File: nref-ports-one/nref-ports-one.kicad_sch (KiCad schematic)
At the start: 155 parts, among them J1 CONN_HEAD, J10 CONN_SPK, J11 POWSW, J12 SBU, J2 DM3AT-SF-PEJM5, J3 09452812561, J4 USB_C_Receptacle, J5 Conn_01x10_Pin, J6 Conn_01x14_Pin, J7 Conn_01x12_Pin, J8 PWR, J9 Conn_01x10_Pin, SW1 SW_Push, U1 TPS7A0533PDBZ, U10 LMR51430, U11 TPS66021YBGR, U12 TLV75518PDBV, U13 TMUXHS4212, U14 EQCO5X31C0-I_6NX, U15 LP5907MFX-1.2, U2 TLV320AIC3100, U3 TXS0108EPW, U4 SN74AVC1T45, U5 TPD4E02B04DQA, U6 TPD4E02B04DQA, U7 TPD4E02B04DQA, U8 FUSB302BMPX, U9 PCA9557RGVR

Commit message: commit various notes / polishing for ports-one and ports-two
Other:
- note added: ""In single-lane mode, only the differential pairs closest to the CC pin are used for data transmission""
- note added: "- if CC2 is pulled down: cable flipped - if CC1 is pulled down: cable unflipped"
- note added: "- if SEL high"
- note added: "- if SEL low"
- note added: "- if SEL low: Port A to Port B - if SEL high: Port A to Port C"
- note added: "A10"
- note added: "A11"
- note added: "A2"
- note added: "A3"
- note added: "B10"
- note added: "B11"
- note added: "B2"
- note added: "B3"
- note added: "pol. swapped on purpose!"
- note removed: "pair swapped on purpose!"

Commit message: ports-one: add TODOs after hw debugging
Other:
- note added: "TODO: P0 is open drain! swap SRC and SINK EN!"
- note added: "TODO: not 3v3 on 66021! (3v3 on 66020)"
- note added: "TODO: remove!!"
- note added: "TODO: remove, internal pulldown"
- note added: "TODO: wrong pinout/footprint"
- note added: "required to start the mechanism"
- note removed: "TODO: possibly 0R"

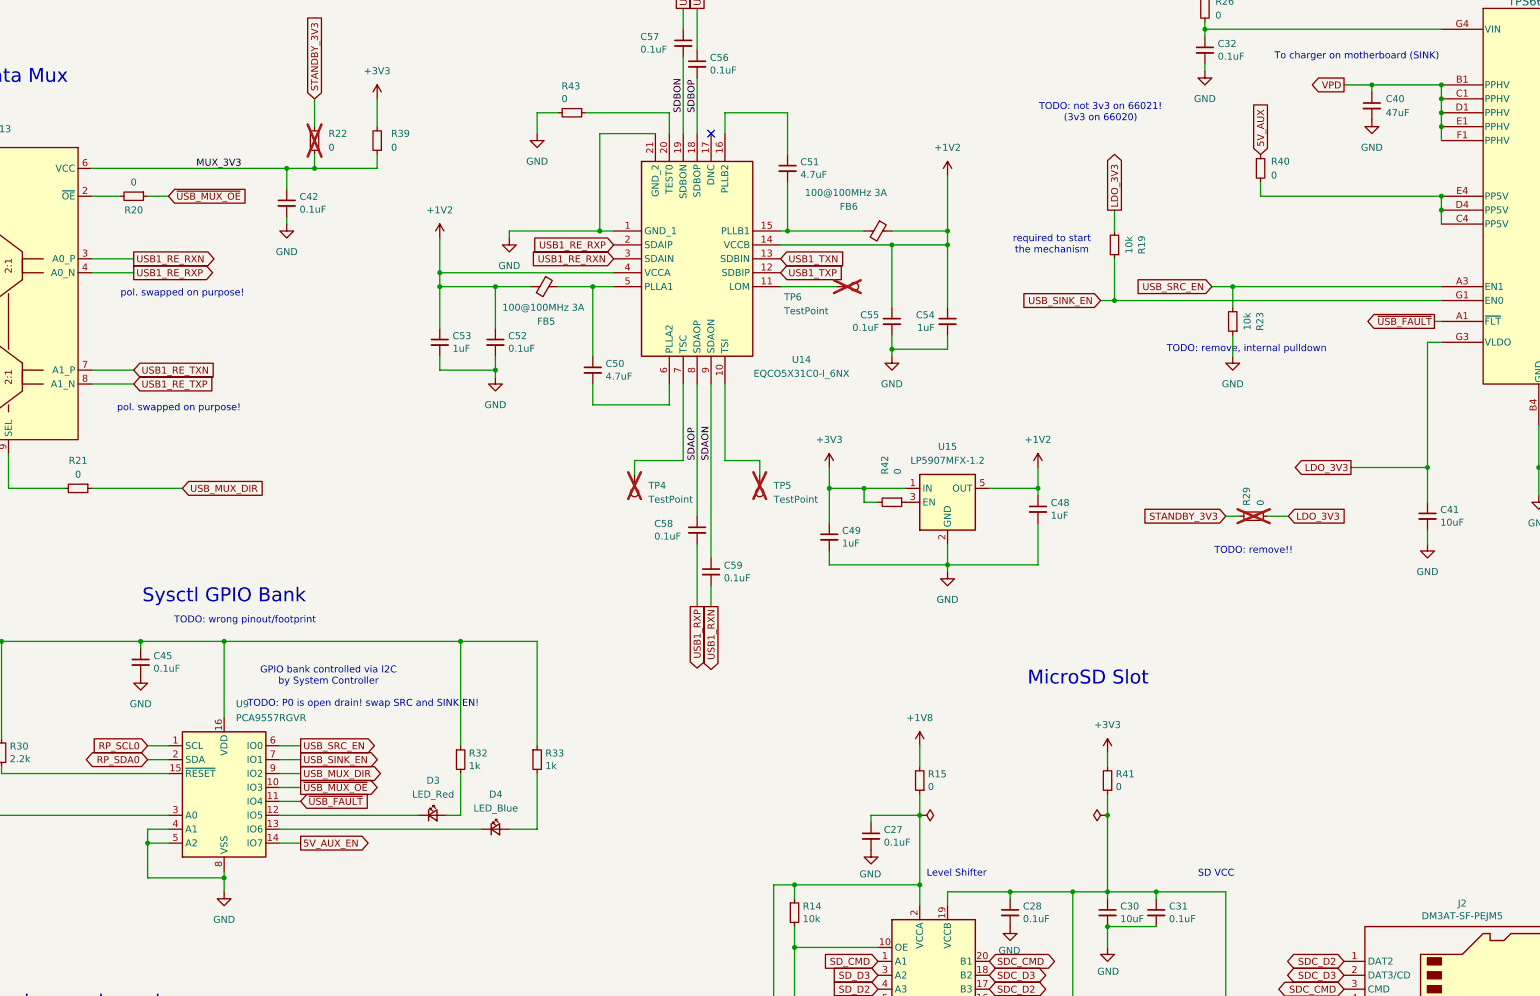
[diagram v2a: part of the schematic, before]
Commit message: ports-one: fix u9 pinout; remove r23
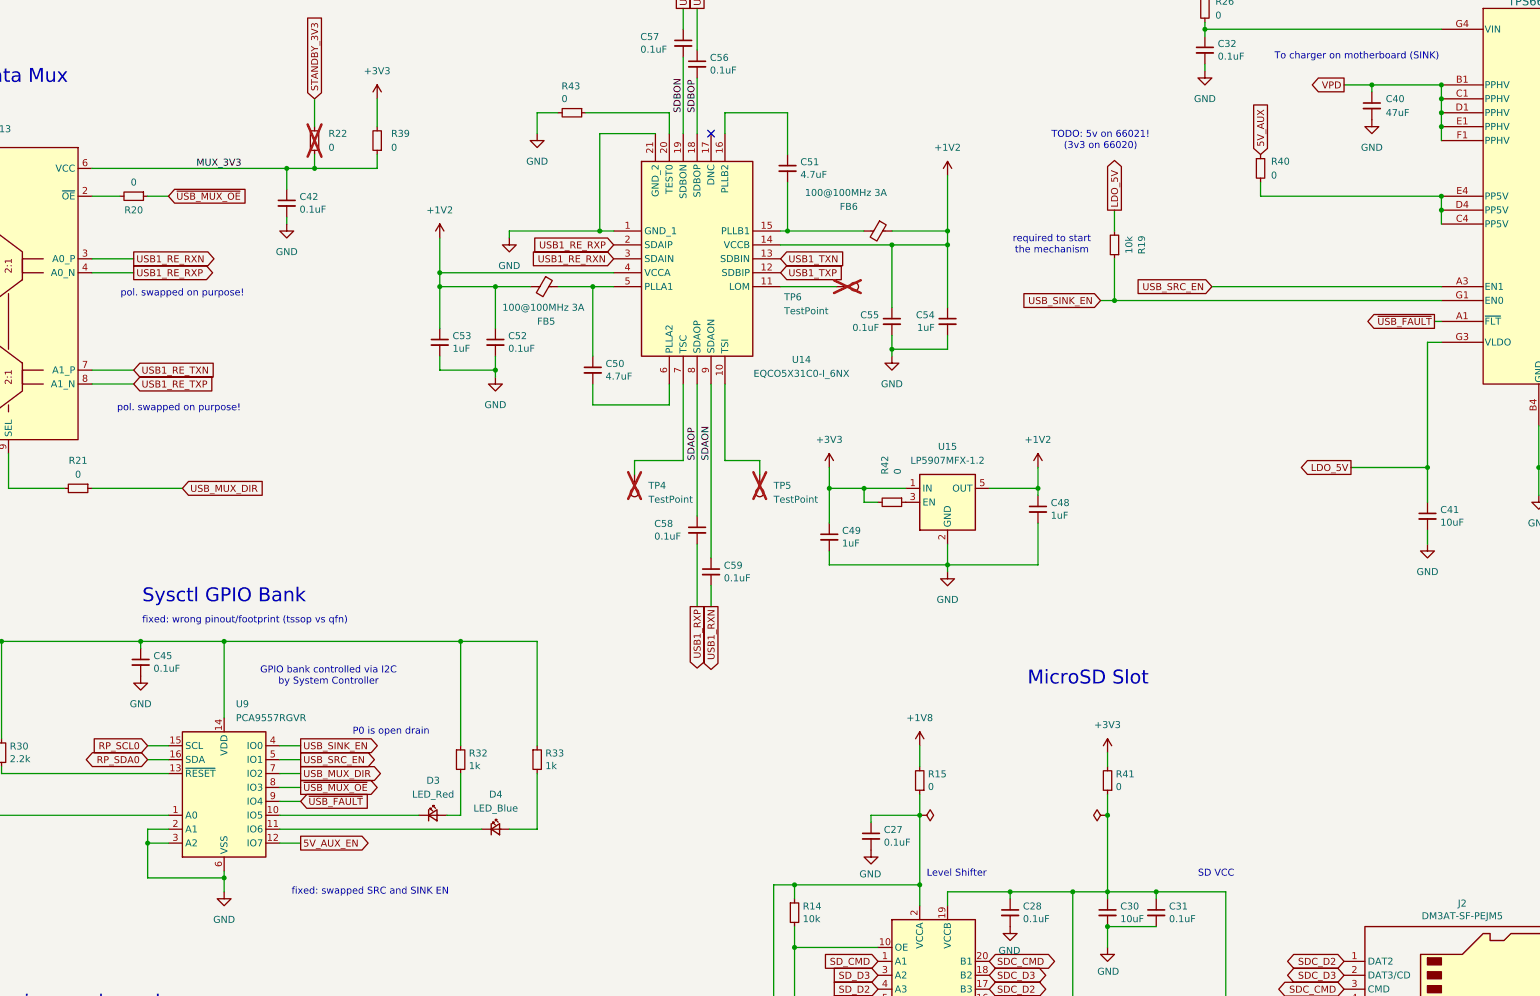
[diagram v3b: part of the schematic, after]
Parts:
- removed R23: 10k, Resistor_SMD:R_0402_1005Metric, symbol Device:R_Small
- removed R29: 0, Resistor_SMD:R_0402_1005Metric, symbol Device:R_Small
- U9: symbol Interface_Expansion:PCA9557PW -> Interface_Expansion:PCA9557BS
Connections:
- net 5V_AUX_EN: now also U9.12 (IO7); no longer U9.14 (IO7)
- net GND: now also U9.2 (A1), U9.3 (A2), U9.6 (VSS); no longer U9.4 (A1), U9.5 (A2), U9.8 (VSS)
- net RP_SCL0: now also U9.15 (SCL); no longer U9.1 (SCL)
- net RP_SDA0: now also U9.16 (SDA); no longer U9.2 (SDA)
- net STANDBY_3V3: now also U9.14 (VDD); no longer U9.16 (VDD)
- net USB_MUX_DIR: now also U9.7 (IO2); no longer U9.9 (IO2)
- net USB_SINK_EN: now also U9.4 (IO0); no longer U9.7 (IO1)
- net USB_SRC_EN: now also U9.5 (IO1); no longer U9.6 (IO0)
- net ~{USB_FAULT}: now also U9.9 (IO4); no longer U9.11 (IO4)
- net ~{USB_MUX_OE}: now also U9.8 (IO3); no longer U9.10 (IO3)
- net at D3.1 (K): now also U9.10 (IO5); no longer U9.12 (IO5)
- net at R30.2: now also U9.13 (~{RESET}); no longer U9.15 (~{RESET})
- net at D4.1 (K): now also U9.11 (IO6); no longer U9.13 (IO6)
- net at R31.2: now also U9.1 (A0); no longer U9.3 (A0)
- net LDO_3V3 renamed LDO_5V
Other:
- note added: "P0 is open drain"
- note added: "TODO: 5v on 66021! (3v3 on 66020)"
- note added: "fixed: swapped SRC and SINK EN"
- note added: "fixed: wrong pinout/footprint (tssop vs qfn)"
- note removed: "TODO: P0 is open drain! swap SRC and SINK EN!"
- note removed: "TODO: not 3v3 on 66021! (3v3 on 66020)"
- note removed: "TODO: remove!!"
- note removed: "TODO: remove, internal pulldown"
- note removed: "TODO: wrong pinout/footprint"
